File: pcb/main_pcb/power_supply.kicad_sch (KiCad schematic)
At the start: 33 parts, among them J12 Screw_Terminal_01x02, J13 Conn_01x02_Male, Q1 Q_PMOS_GDS, SW1 SW_SPDT, U4 LM1117-3.3, U5 TPIC74101

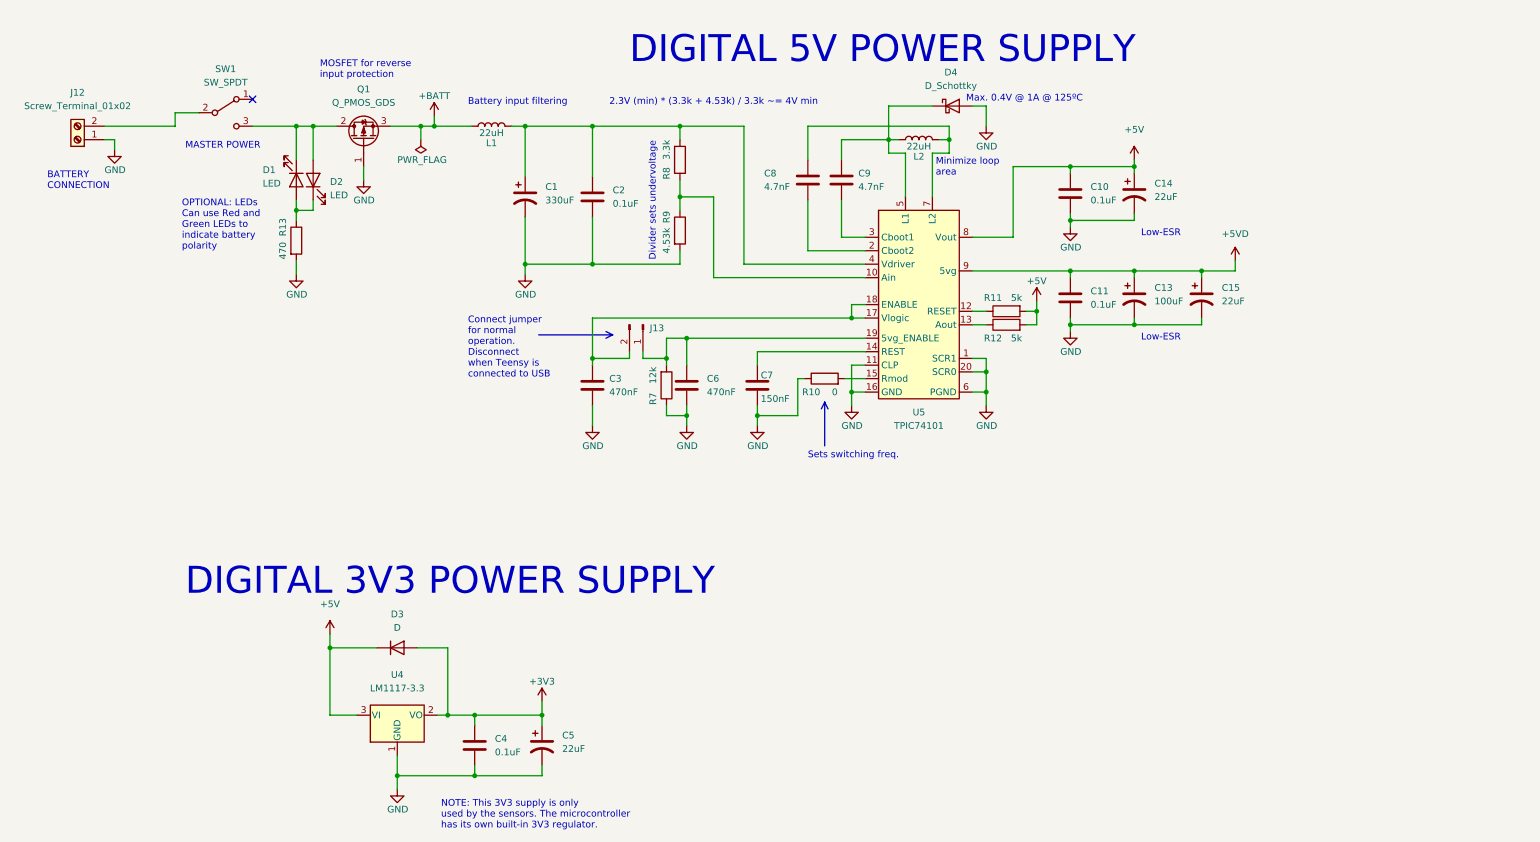
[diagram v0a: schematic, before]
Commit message: deleted digital 5V power supply
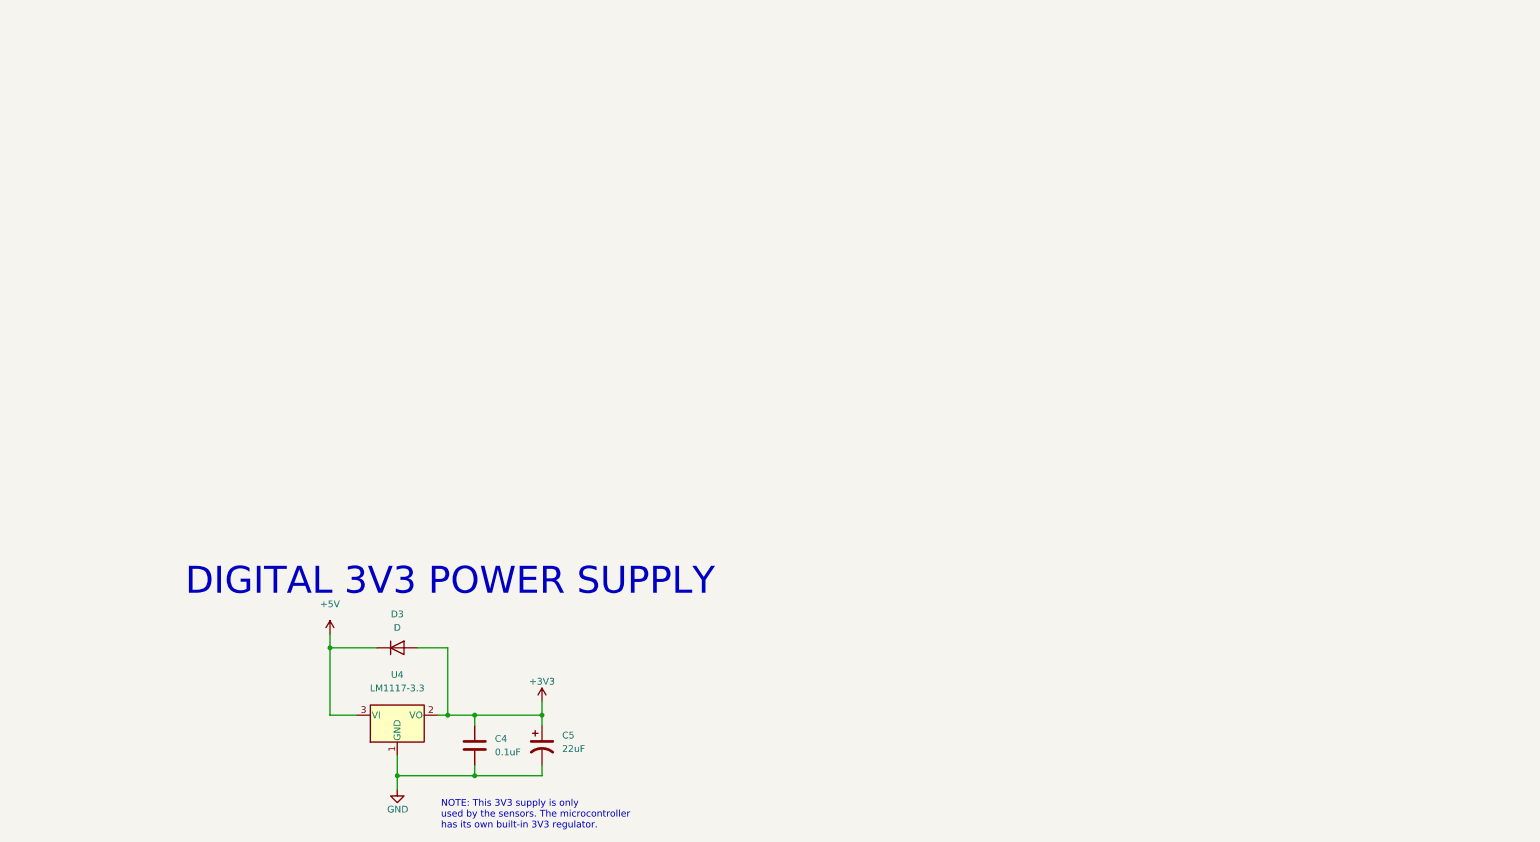
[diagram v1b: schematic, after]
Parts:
- removed C1: 330uF, Capacitor_SMD:CP_Elec_10x10.5, symbol Device:C_Polarized_US
- removed C10, C11, C2: 0.1uF, Capacitor_SMD:C_0603_1608Metric_Pad1.08x0.95mm_HandSolder, symbol Device:C
- removed C13: 100uF, Capacitor_SMD:CP_Elec_8x10.5, symbol Device:C_Polarized_US
- removed C14, C15: 22uF, Capacitor_SMD:CP_Elec_8x10.5, symbol Device:C_Polarized_US
- removed C3, C6: 470nF, Capacitor_SMD:C_0603_1608Metric_Pad1.08x0.95mm_HandSolder, symbol Device:C
- removed C7: 150nF, Capacitor_SMD:C_0603_1608Metric_Pad1.08x0.95mm_HandSolder, symbol Device:C
- removed C8, C9: 4.7nF, Capacitor_SMD:C_0603_1608Metric_Pad1.08x0.95mm_HandSolder, symbol Device:C
- removed D1, D2: LED, LED_THT:LED_D5.0mm, symbol Device:LED
- removed D4: D_Schottky, Diode_SMD:D_TUMD2, symbol Device:D_Schottky
- removed J12: Screw_Terminal_01x02, TerminalBlock:TerminalBlock_bornier-2_P5.08mm, symbol Connector:Screw_Terminal_01x02
- removed J13: Conn_01x02_Male, Connector_PinHeader_2.54mm:PinHeader_1x02_P2.54mm_Vertical, symbol Connector:Conn_01x02_Male
- removed L1, L2: 22uH, custom_footprints:L_SRR1050HA_Bourns, symbol Device:L
- removed Q1: Q_PMOS_GDS, Package_TO_SOT_SMD:TO-263-3_TabPin2, symbol Device:Q_PMOS_GDS
- removed R10: 0, Resistor_SMD:R_0603_1608Metric_Pad0.98x0.95mm_HandSolder, symbol Device:R
- removed R11, R12: 5k, Resistor_SMD:R_0603_1608Metric_Pad0.98x0.95mm_HandSolder, symbol Device:R
- removed R13: 470, Resistor_SMD:R_0603_1608Metric_Pad0.98x0.95mm_HandSolder, symbol Device:R
- removed R7: 12k, Resistor_SMD:R_0603_1608Metric_Pad0.98x0.95mm_HandSolder, symbol Device:R
- removed R8: 3.3k, Resistor_SMD:R_0603_1608Metric_Pad0.98x0.95mm_HandSolder, symbol Device:R
- removed R9: 4.53k, Resistor_SMD:R_0603_1608Metric_Pad0.98x0.95mm_HandSolder, symbol Device:R
- removed SW1: SW_SPDT, custom_footprints:SW_SPDT_NKK_MS12AANW03, symbol Switch:SW_SPDT
- removed U5: TPIC74101, custom_footprints:HTSSOP-20-1EP_4.4x6.5mm_P0.65mm_EP3.4x6.5mm_ThermalVias, symbol sym_library:TPIC74101
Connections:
- no-connect marks 1 -> 0
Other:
- note removed: "2.3V (min) * (3.3k + 4.53k) / 3.3k ~= 4V min"
- note removed: "BATTERY CONNECTION"
- note removed: "Battery input filtering"
- note removed: "Connect jumper for normal operation. Disconnect when Teensy is connected to USB"
- note removed: "DIGITAL 5V POWER SUPPLY"
- note removed: "Divider sets undervoltage"
- note removed: "Low-ESR"
- note removed: "MASTER POWER"
- note removed: "MOSFET for reverse input protection"
- note removed: "Max. 0.4V @ 1A @ 125ºC"
- note removed: "Minimize loop area"
- note removed: "OPTIONAL: LEDs Can use Red and Green LEDs to indicate battery polarity"
- note removed: "Sets switching freq."

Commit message: title change
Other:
- note added: "DIGITAL 3V3 POWER SUPPLY (SAMPLE)"
- note added: "DIGITAL 3V3/3V POWER SUPPLY"
- note removed: "DIGITAL 3V3 POWER SUPPLY"
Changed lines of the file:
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@@
     (stroke (width 0) (type default) (color 0 0 0 0))
   )
-  (text "DIGITAL 3V3 POWER SUPPLY" (at 46.355 132.715 0)
+  (text "DIGITAL 3V3 POWER SUPPLY (SAMPLE)" (at 31.75 133.35 0)
     (effects (font (size 5.08 5.08)) (justify left bottom))
   )
@@
     (effects (font (size 1.27 1.27)) (justify left bottom))
   )
+  (text "DIGITAL 3V3/3V POWER SUPPLY" (at 80.01 30.48 0)
+    (effects (font (size 5.08 5.08)) (justify left bottom))
+  )
   (symbol (lib_id "power:+3V3") (at 113.665 152.4 0) (unit 1)

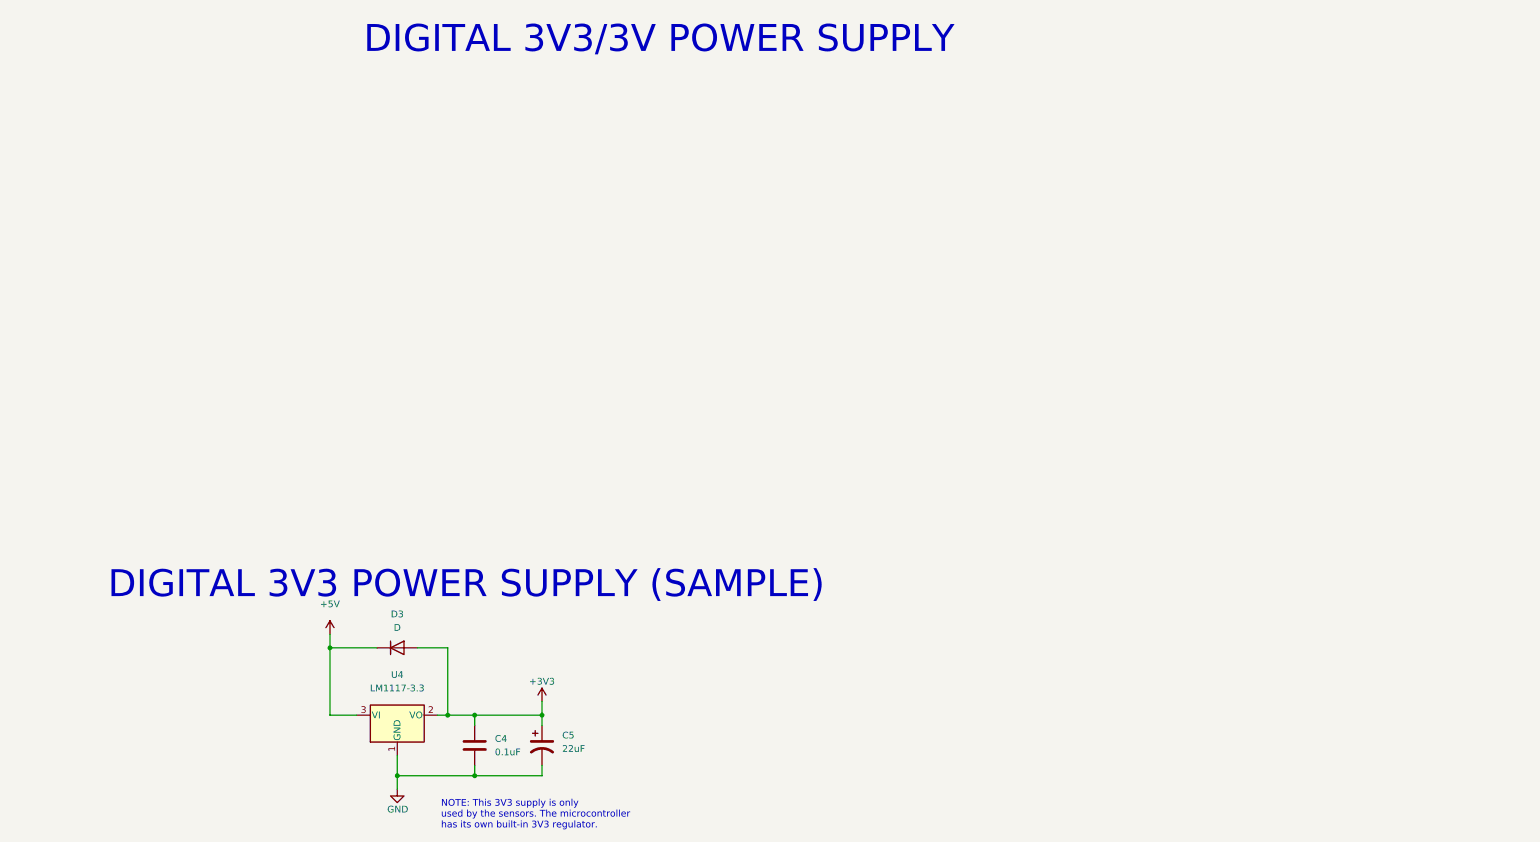
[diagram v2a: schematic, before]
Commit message: Deleted old 3v3 power supply
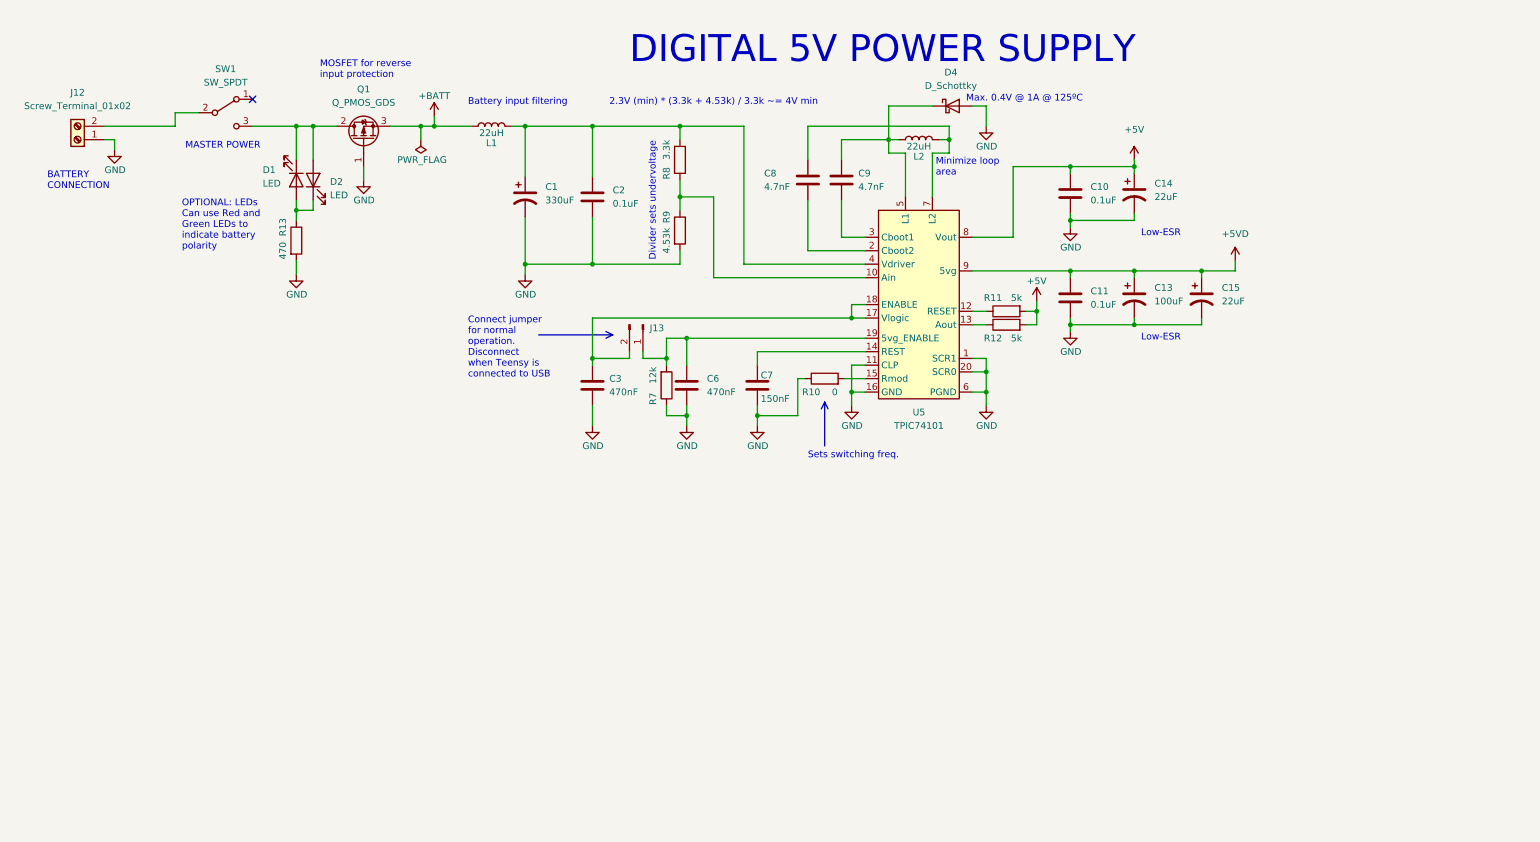
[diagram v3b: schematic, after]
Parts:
- removed C4: 0.1uF, Capacitor_SMD:C_0603_1608Metric_Pad1.08x0.95mm_HandSolder, symbol Device:C
- removed C5: 22uF, Capacitor_SMD:CP_Elec_8x10.5, symbol Device:C_Polarized_US
- removed D3: D, Diode_SMD:D_0805_2012Metric, symbol Device:D
- removed U4: LM1117-3.3, Package_TO_SOT_SMD:SOT-223-3_TabPin2, symbol Regulator_Linear:LM1117-3.3
- added C1: 330uF, Capacitor_SMD:CP_Elec_10x10.5, symbol Device:C_Polarized_US
- added C10, C11, C2: 0.1uF, Capacitor_SMD:C_0603_1608Metric_Pad1.08x0.95mm_HandSolder, symbol Device:C
- added C13: 100uF, Capacitor_SMD:CP_Elec_8x10.5, symbol Device:C_Polarized_US
- added C14, C15: 22uF, Capacitor_SMD:CP_Elec_8x10.5, symbol Device:C_Polarized_US
- added C3, C6: 470nF, Capacitor_SMD:C_0603_1608Metric_Pad1.08x0.95mm_HandSolder, symbol Device:C
- added C7: 150nF, Capacitor_SMD:C_0603_1608Metric_Pad1.08x0.95mm_HandSolder, symbol Device:C
- added C8, C9: 4.7nF, Capacitor_SMD:C_0603_1608Metric_Pad1.08x0.95mm_HandSolder, symbol Device:C
- added D1, D2: LED, LED_THT:LED_D5.0mm, symbol Device:LED
- added D4: D_Schottky, Diode_SMD:D_TUMD2, symbol Device:D_Schottky
- added J12: Screw_Terminal_01x02, TerminalBlock:TerminalBlock_bornier-2_P5.08mm, symbol Connector:Screw_Terminal_01x02
- added J13: Conn_01x02_Male, Connector_PinHeader_2.54mm:PinHeader_1x02_P2.54mm_Vertical, symbol Connector:Conn_01x02_Male
- added L1, L2: 22uH, custom_footprints:L_SRR1050HA_Bourns, symbol Device:L
- added Q1: Q_PMOS_GDS, Package_TO_SOT_SMD:TO-263-3_TabPin2, symbol Device:Q_PMOS_GDS
- added R10: 0, Resistor_SMD:R_0603_1608Metric_Pad0.98x0.95mm_HandSolder, symbol Device:R
- added R11, R12: 5k, Resistor_SMD:R_0603_1608Metric_Pad0.98x0.95mm_HandSolder, symbol Device:R
- added R13: 470, Resistor_SMD:R_0603_1608Metric_Pad0.98x0.95mm_HandSolder, symbol Device:R
- added R7: 12k, Resistor_SMD:R_0603_1608Metric_Pad0.98x0.95mm_HandSolder, symbol Device:R
- added R8: 3.3k, Resistor_SMD:R_0603_1608Metric_Pad0.98x0.95mm_HandSolder, symbol Device:R
- added R9: 4.53k, Resistor_SMD:R_0603_1608Metric_Pad0.98x0.95mm_HandSolder, symbol Device:R
- added SW1: SW_SPDT, custom_footprints:SW_SPDT_NKK_MS12AANW03, symbol Switch:SW_SPDT
- added U5: TPIC74101, custom_footprints:HTSSOP-20-1EP_4.4x6.5mm_P0.65mm_EP3.4x6.5mm_ThermalVias, symbol sym_library:TPIC74101
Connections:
- net +5V: now also C10.1, C14.1, R11.2, R12.2, U5.8 (Vout)
- net GND: now also C1.2, C10.2, C11.2, C13.2, C14.2, C15.2, C2.2, C3.2, C6.2, C7.2, D4.2 (A), J12.1 (Pin_1), Q1.1 (G), R10.1, R13.2, R7.1, R9.2, U5.1 (SCR1), U5.11 (CLP), U5.16 (GND), U5.20 (SCR0), U5.21 (PAD), U5.6 (PGND)
- new net: C1.1, C2.1, L1.2, R8.2, U5.4 (Vdriver)
- new net: D1.1 (K), D2.2 (A), Q1.2 (D), SW1.3 (C)
- new net: R8.1, R9.1, U5.10 (Ain)
- new net: R11.1, U5.12 (RESET)
- new net: R12.1, U5.13 (Aout)
- new net: C7.1, U5.14 (REST)
- new net: R10.2, U5.15 (Rmod)
- new net: C3.1, J13.2 (Pin_2), U5.17 (Vlogic), U5.18 (ENABLE)
- new net: C6.1, J13.1 (Pin_1), R7.2, U5.19 (5vg_ENABLE)
- new net: C8.2, U5.2 (Cboot2)
- new net: C9.2, U5.3 (Cboot1)
- new net: C9.1, D4.1 (K), L2.1, U5.5 (L1)
- new net: C8.1, L2.2, U5.7 (L2)
- new net: J12.2 (Pin_2), SW1.2 (B)
- new net: D1.2 (A), D2.1 (K), R13.1
- new net +5VD: C11.1, C13.1, C15.1, U5.9 (5vg)
- new net +BATT: L1.1, Q1.3 (S)
- no-connect marks 0 -> 1
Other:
- note added: "2.3V (min) * (3.3k + 4.53k) / 3.3k ~= 4V min"
- note added: "BATTERY CONNECTION"
- note added: "Battery input filtering"
- note added: "Connect jumper for normal operation. Disconnect when Teensy is connected to USB"
- note added: "DIGITAL 5V POWER SUPPLY"
- note added: "Divider sets undervoltage"
- note added: "Low-ESR"
- note added: "MASTER POWER"
- note added: "MOSFET for reverse input protection"
- note added: "Max. 0.4V @ 1A @ 125ºC"
- note added: "Minimize loop area"
- note added: "OPTIONAL: LEDs Can use Red and Green LEDs to indicate battery polarity"
- note added: "Sets switching freq."
- note removed: "DIGITAL 3V3 POWER SUPPLY (SAMPLE)"
- note removed: "DIGITAL 3V3/3V POWER SUPPLY"
- note removed: "NOTE: This 3V3 supply is only used by the sensors. The microcontroller has its own built-in 3V3 regulator."

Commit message: small changes
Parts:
- added C16, C17, C18, C19, C20: C, symbol Device:C
- added L3: L, symbol Device:L
- added U1: LM3151/2/3, custom_footprints:HTSSOP-20-1EP_4.4x6.5mm_P0.65mm_EP3.4x6.5mm_ThermalVias, symbol sym_library:TPIC74101
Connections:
- net GND renamed +3.3V
- net +3.3V: now also C17.1, C17.2, C18.2, C19.2, C20.1, C20.2, L3.1, U1.1 (VCC), U1.10 (SW), U1.11 (HG), U1.12 (BST), U1.13 (LG), U1.14 (PGND), U1.2 (VIN), U1.5 (SGND), U1.6 (SS)
- new net: C18.1, L3.2, U1.4 (FB)
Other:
- note added: "SIMPLE SWITCHER CONTROLLER"
